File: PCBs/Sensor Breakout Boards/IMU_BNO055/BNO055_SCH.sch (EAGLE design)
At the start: 6 parts, among them U1 BNO055

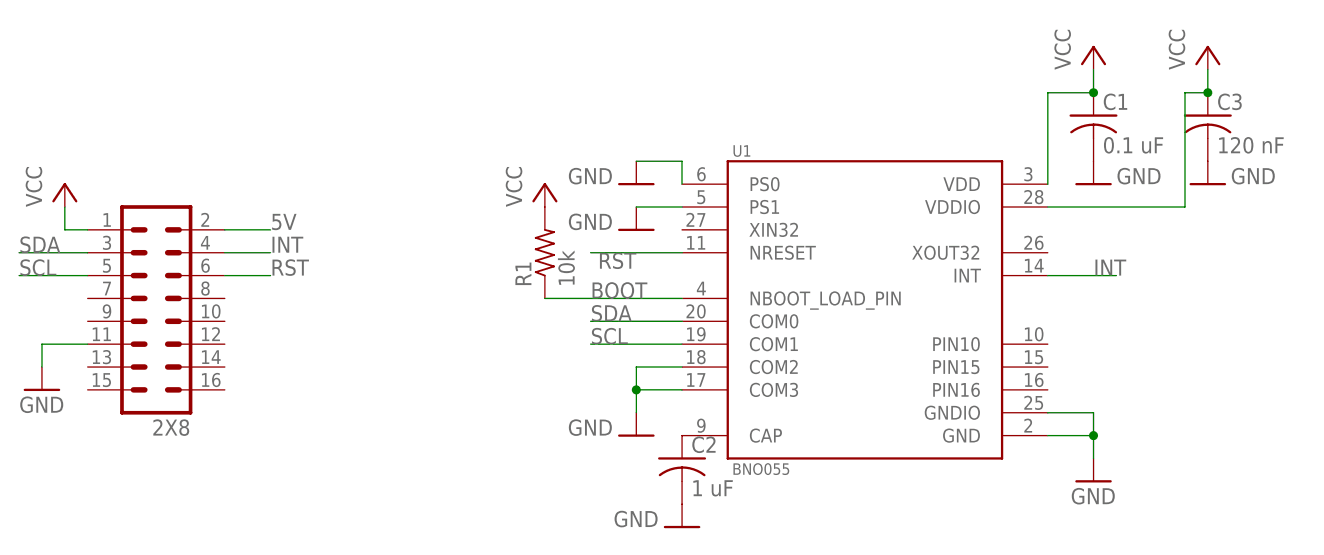
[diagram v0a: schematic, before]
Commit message: Moved the caps to actually be useful
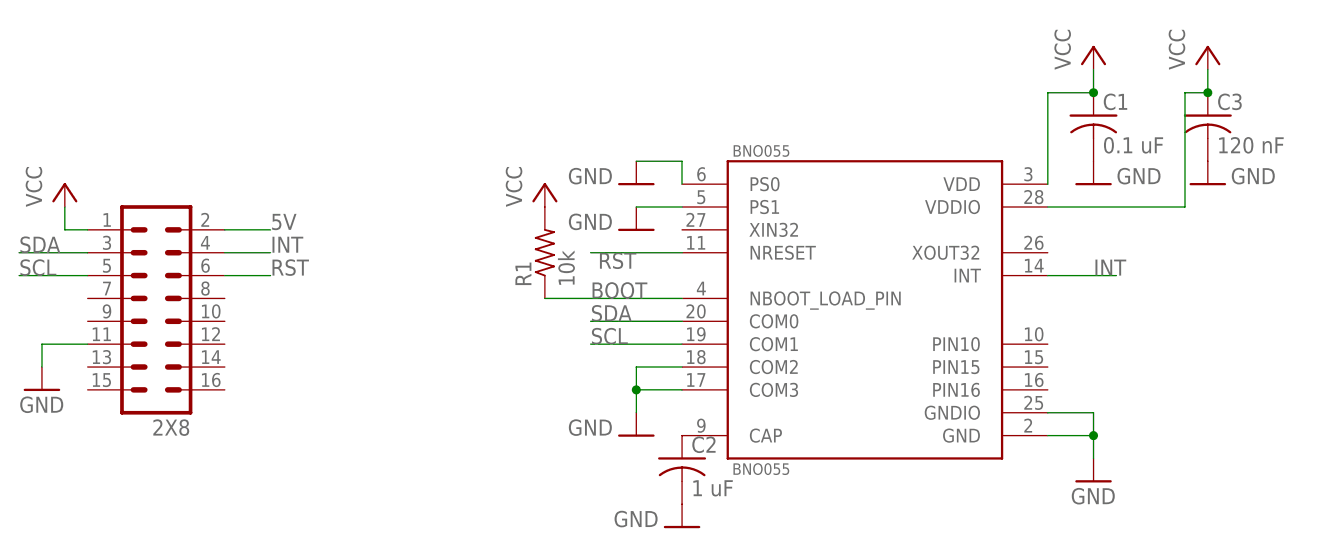
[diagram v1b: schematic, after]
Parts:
- renumbered U1 to BNO055
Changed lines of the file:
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@@
 </variantdefs>
 <classes>
-<class number="0" name="default" width="0" drill="0">
+<class number="0" name="default" width="0.3048" drill="0.508">
+<clearance class="0" value="0.254"/>
 </class>
 </classes>
 <parts>
-<part name="U1" library="BNO055" deviceset="BNO055" device=""/>
+<part name="BNO055" library="BNO055" deviceset="BNO055" device=""/>
 <part name="P+1" library="supply1" library_urn="urn:adsk.eagle:library:371" deviceset="VCC" device=""/>
 <part name="P+2" library="supply1" library_urn="urn:adsk.eagle:library:371" deviceset="VCC" device=""/>
@@
 </plain>
 <instances>
-<instance part="U1" gate="G$1" x="55.88" y="55.88" smashed="yes">
+<instance part="BNO055" gate="G$1" x="55.88" y="55.88" smashed="yes">
 <attribute name="NAME" x="41.1403" y="71.6362" size="1.270659375" layer="95"/>
 <attribute name="VALUE" x="41.1193" y="36.2838" size="1.27248125" layer="96"/>
@@
 <net name="VCC" class="0">
 <segment>
-<pinref part="U1" gate="G$1" pin="VDD"/>
+<pinref part="BNO055" gate="G$1" pin="VDD"/>
 <wire x1="76.2" y1="68.58" x2="76.2" y2="78.74" width="0.1524" layer="91"/>
 <wire x1="76.2" y1="78.74" x2="81.28" y2="78.74" width="0.1524" layer="91"/>
@@
 </segment>
 <segment>
-<pinref part="U1" gate="G$1" pin="VDDIO"/>
+<pinref part="BNO055" gate="G$1" pin="VDDIO"/>
 <wire x1="76.2" y1="66.04" x2="91.44" y2="66.04" width="0.1524" layer="91"/>
 <wire x1="91.44" y1="66.04" x2="91.44" y2="78.74" width="0.1524" layer="91"/>
@@
 <pinref part="GND2" gate="1" pin="GND"/>
 <wire x1="81.28" y1="40.64" x2="81.28" y2="38.1" width="0.1524" layer="91"/>
-<pinref part="U1" gate="G$1" pin="GNDIO"/>
+<pinref part="BNO055" gate="G$1" pin="GNDIO"/>
 <wire x1="76.2" y1="43.18" x2="81.28" y2="43.18" width="0.1524" layer="91"/>
 <wire x1="81.28" y1="43.18" x2="81.28" y2="40.64" width="0.1524" layer="91"/>
 <junction x="81.28" y="40.64"/>
-<pinref part="U1" gate="G$1" pin="GND"/>
+<pinref part="BNO055" gate="G$1" pin="GND"/>
 <wire x1="76.2" y1="40.64" x2="81.28" y2="40.64" width="0.1524" layer="91"/>
 </segment>
@@
 </segment>
 <segment>
-<pinref part="U1" gate="G$1" pin="COM2"/>
+<pinref part="BNO055" gate="G$1" pin="COM2"/>
 <wire x1="35.56" y1="48.26" x2="30.48" y2="48.26" width="0.1524" layer="91"/>
-<pinref part="U1" gate="G$1" pin="COM3"/>
+<pinref part="BNO055" gate="G$1" pin="COM3"/>
 <wire x1="35.56" y1="45.72" x2="30.48" y2="45.72" width="0.1524" layer="91"/>
 <wire x1="30.48" y1="45.72" x2="30.48" y2="43.18" width="0.1524" layer="91"/>
@@
 </segment>
 <segment>
-<pinref part="U1" gate="G$1" pin="PS1"/>
+<pinref part="BNO055" gate="G$1" pin="PS1"/>
 <pinref part="GND6" gate="1" pin="GND"/>
 <wire x1="35.56" y1="66.04" x2="30.48" y2="66.04" width="0.1524" layer="91"/>
 </segment>
 <segment>
-<pinref part="U1" gate="G$1" pin="PS0"/>
+<pinref part="BNO055" gate="G$1" pin="PS0"/>
 <wire x1="35.56" y1="68.58" x2="35.56" y2="71.12" width="0.1524" layer="91"/>
 <pinref part="GND7" gate="1" pin="GND"/>
@@
 <net name="N$3" class="0">
 <segment>
-<pinref part="U1" gate="G$1" pin="CAP"/>
+<pinref part="BNO055" gate="G$1" pin="CAP"/>
 <pinref part="C2" gate="G$1" pin="1"/>
 </segment>
@@
 <net name="BOOT" class="0">
 <segment>
-<pinref part="U1" gate="G$1" pin="NBOOT_LOAD_PIN"/>
+<pinref part="BNO055" gate="G$1" pin="NBOOT_LOAD_PIN"/>
 <label x="25.4" y="55.88" size="1.778" layer="95"/>
 <pinref part="R1" gate="G$1" pin="1"/>
@@
 </segment>
 <segment>
-<pinref part="U1" gate="G$1" pin="COM0"/>
+<pinref part="BNO055" gate="G$1" pin="COM0"/>
 <wire x1="35.56" y1="53.34" x2="25.4" y2="53.34" width="0.1524" layer="91"/>
 <label x="25.4" y="53.34" size="1.778" layer="95"/>
@@
 </segment>
 <segment>
-<pinref part="U1" gate="G$1" pin="COM1"/>
+<pinref part="BNO055" gate="G$1" pin="COM1"/>
 <wire x1="35.56" y1="50.8" x2="25.4" y2="50.8" width="0.1524" layer="91"/>
 <label x="25.4" y="50.8" size="1.778" layer="95"/>
@@
 <net name="INT" class="0">
 <segment>
-<pinref part="U1" gate="G$1" pin="INT"/>
+<pinref part="BNO055" gate="G$1" pin="INT"/>
 <wire x1="76.2" y1="58.42" x2="83.82" y2="58.42" width="0.1524" layer="91"/>
 <label x="81.28" y="58.42" size="1.778" layer="95"/>
@@
 </segment>
 <segment>
-<pinref part="U1" gate="G$1" pin="NRESET"/>
+<pinref part="BNO055" gate="G$1" pin="NRESET"/>
 <wire x1="35.56" y1="60.96" x2="25.4" y2="60.96" width="0.1524" layer="91"/>
 <label x="30.48" y="60.96" size="1.778" layer="95" rot="R180"/>
